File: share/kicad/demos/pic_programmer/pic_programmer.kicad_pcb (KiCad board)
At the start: 2 copper layers, 160 x 99.1 mm, 63 parts, among them J1 DB9-FEMAL, P1 CONN_2, P101 CONN_1, P102 CONN_1, P103 CONN_1, P104 CONN_1, P105 CONN_1, P106 CONN_1, P2 SUPP28, P3 SUPP40, Q1 BC237, Q2 BC307, Q3 BC307, U1 24Cxx, U2 74HC125, U3 7805, U4 LT1373, U5 PIC_18_PINS, U6 PIC_8_PINS

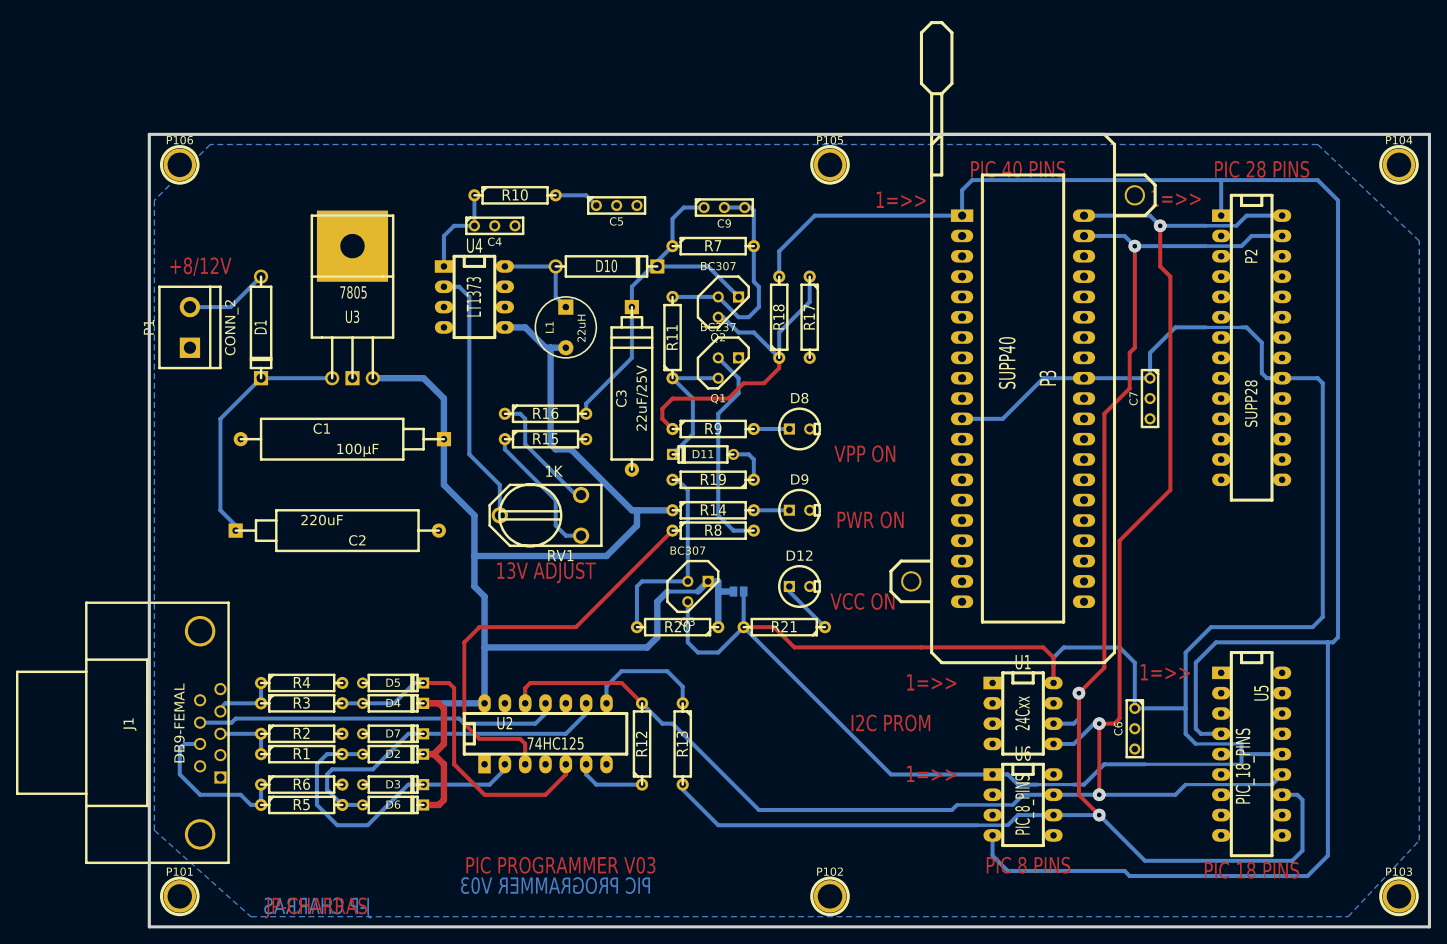
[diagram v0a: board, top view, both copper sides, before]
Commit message: Remove KiCad V4.0.7
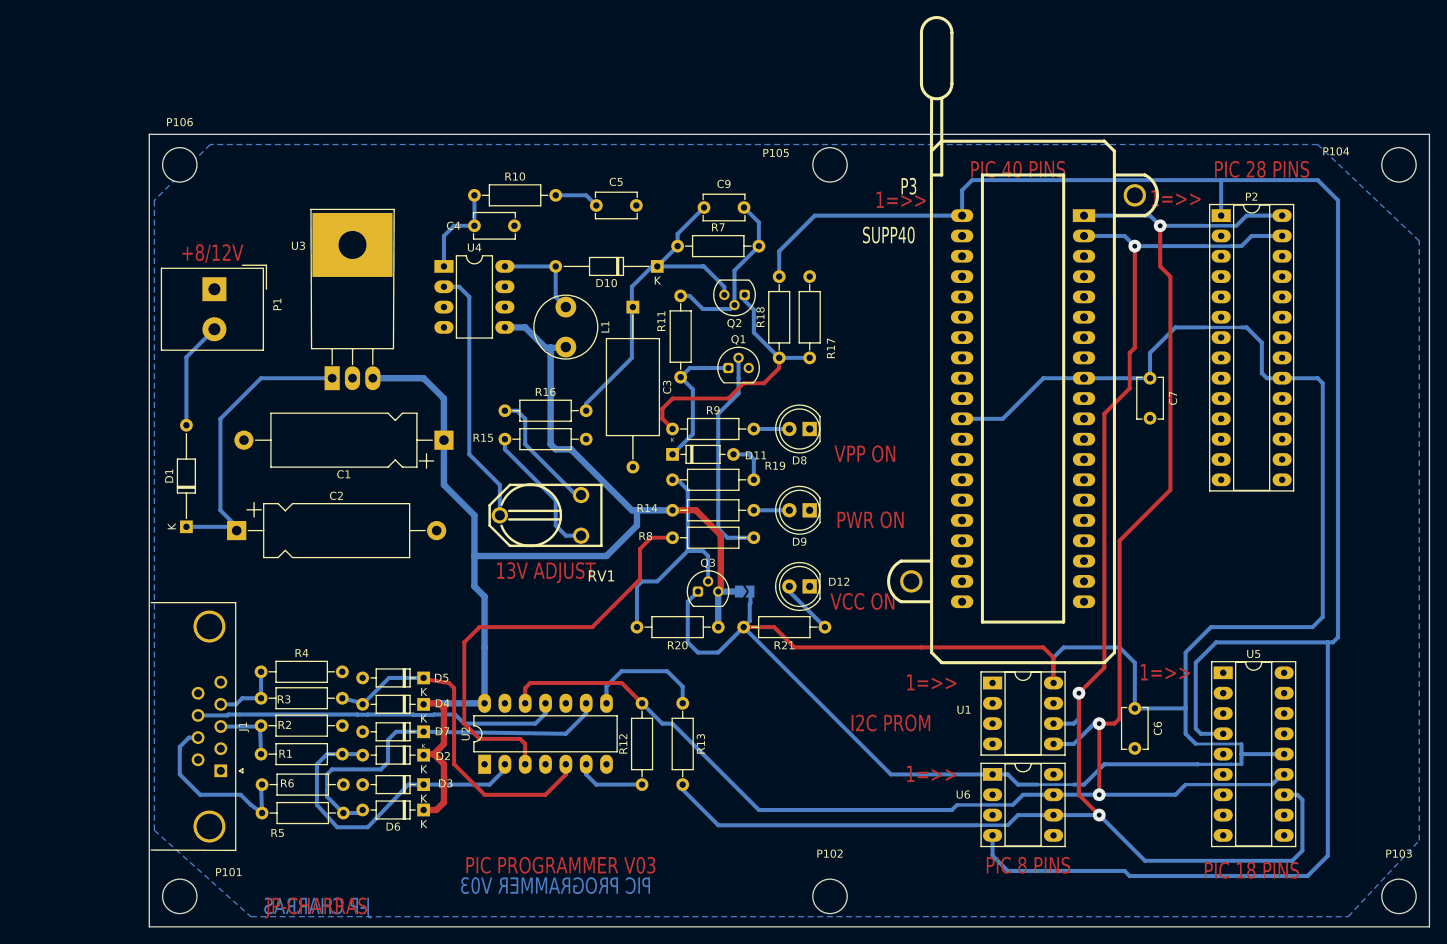
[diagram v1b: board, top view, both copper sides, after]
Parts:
- C1, C2: footprint discret:CP10 -> Capacitor_THT:CP_Axial_L18.0mm_D6.5mm_P25.00mm_Horizontal
- C3: footprint discret:CP8 -> Capacitors_THT:C_Axial_L12.0mm_D6.5mm_P20.00mm_Horizontal
- C4, C5, C6, C7: footprint discret:C1-1 -> Capacitor_THT:C_Disc_D5.1mm_W3.2mm_P5.00mm
- C9: value 22OnF -> 220nF; footprint discret:C1-1 -> Capacitor_THT:C_Disc_D5.1mm_W3.2mm_P5.00mm
- D1, D10: footprint discret:D5 -> Diode_THT:D_DO-35_SOD27_P12.70mm_Horizontal
- D11, D2, D3, D4, D5, D6, D7: footprint discret:D3 -> Diode_THT:D_DO-35_SOD27_P7.62mm_Horizontal
- D12, D8, D9: footprint discret:LEDV -> LED_THT:LED_D5.0mm
- J1: footprint connect:DB9FC -> Connector_Dsub:DSUB-9_Female_Horizontal_P2.77x2.84mm_EdgePinOffset7.70mm_Housed_MountingHolesOffset9.12mm
- JP1: footprint connect:GS2 -> Jumper:SolderJumper-2_P1.3mm_Open_TrianglePad1.0x1.5mm
- L1: footprint inductors:INDUCTOR_V -> Inductor_THT:L_Radial_D7.8mm_P5.00mm_Fastron_07HCP
- P1: footprint connect:bornier2 -> TerminalBlock_Altech:Altech_AK300_1x02_P5.00mm_45-Degree
- P101, P102, P103, P104, P105, P106: footprint footprints:1pin-4 -> MountingHole:MountingHole_4.3mm_M4
- P2: footprint dip_sockets:DIP-28__300_ELL -> Package_DIP:DIP-28_W7.62mm_Socket_LongPads
- P3: footprint sockets:40tex-Ell600 -> footprints:40tex-Ell600
- Q1, Q2, Q3: footprint discret:TO92 -> Package_TO_SOT_THT:TO-92
- R1, R10, R11, R12, R13, R14, R15, R16, R17, R18, R19, R2, R20, R21, R3, R4, R5, R6, R7, R8, R9: footprint discret:R4 -> Resistor_THT:R_Axial_DIN0207_L6.3mm_D2.5mm_P10.16mm_Horizontal
- RV1: footprint discret:RV2X4 -> footprints:RV2X4
- U1, U6: footprint dip_sockets:DIP-8__300_ELL -> Package_DIP:DIP-8_W7.62mm_Socket_LongPads
- U2: footprint dip_sockets:DIP-14__300_ELL -> Package_DIP:DIP-14_W7.62mm_LongPads
- U3: footprint discret:LM78XX -> Package_TO_SOT_THT:TO-220-3_Horizontal_TabDown
- U4: footprint dip_sockets:DIP-8__300_ELL -> Package_DIP:DIP-8_W7.62mm_LongPads
- U5: footprint dip_sockets:DIP-18__300_ELL -> Package_DIP:DIP-18_W7.62mm_Socket_LongPads
- moved D1 26.6 mm to (78.3, 89.7), turned to 90 degrees
- moved P3 25.3 mm to (175.3, 50.8), turned to 0 degrees
- moved P2 16.9 mm to (207.6, 50.8), turned to 0 degrees
- moved C1 12.7 mm to (110.5, 78.9)
- moved C2 12.6 mm to (84.6, 90.2)
- moved U5 10.8 mm to (207.9, 108.0), turned to 0 degrees
- moved C3 10.2 mm to (134.1, 62.2)
- moved U2 8.52 mm to (115.6, 119.4), turned to 90 degrees
- moved D10 6.35 mm to (137.2, 57.1), turned to 180 degrees
- moved RV1 5.68 mm to (127.6, 90.8)
- moved P1 5.67 mm to (81.8, 60.0), turned to -90 degrees
- moved U1 5.39 mm to (179.1, 109.2), turned to 0 degrees
- moved U4 5.39 mm to (110.5, 57.1), turned to 0 degrees
- moved U6 5.39 mm to (179.1, 120.7), turned to 0 degrees
- moved R4 5.27 mm to (87.6, 107.8)
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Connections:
- net /CTS renamed /PC-DATA-IN
- net /DTR renamed /PC-DATA-OUT
- net /TXD renamed /VPP_ON
- net /pic_sockets/CLOCK-RB6 renamed /CLOCK-RB6
- net /pic_sockets/DATA-RB7 renamed /DATA-RB7
- net /pic_sockets/VPP-MCLR renamed /VPP/MCLR
- D1 pad 1: Net-(D1-Pad1) -> Net-(C2-Pad1)
- D1 pad 2: Net-(C2-Pad1) -> Net-(D1-Pad2)
- D10 pad 1: Net-(D10-Pad1) -> VPP
- D10 pad 2: VPP -> Net-(D10-Pad2)
- D12 pad 1: Net-(D12-Pad1) -> GND
- D12 pad 2: GND -> Net-(D12-Pad2)
- D2 pad 1: Net-(D2-Pad1) -> VCC
- D2 pad 2: VCC -> Net-(D2-Pad2)
- D3 pad 1: GND -> Net-(D2-Pad2)
- D3 pad 2: Net-(D2-Pad1) -> GND
- D4 pad 1: Net-(D4-Pad1) -> VCC
- D4 pad 2: VCC -> Net-(D4-Pad2)
- D5 pad 1: GND -> Net-(D4-Pad2)
- D5 pad 2: Net-(D4-Pad1) -> GND
- D6 pad 1: Net-(D6-Pad1) -> VCC
- D6 pad 2: VCC -> Net-(D6-Pad2)
- D7 pad 1: GND -> Net-(D6-Pad2)
- D7 pad 2: Net-(D6-Pad1) -> GND
- D8 pad 1: Net-(D8-Pad1) -> GND
- D8 pad 2: GND -> Net-(D8-Pad2)
- D9 pad 1: Net-(D9-Pad1) -> GND
- D9 pad 2: GND -> Net-(D9-Pad2)
- J1 pad 1: (no net) -> unconnected-(J1-Pad1)
- J1 pad 2: (no net) -> unconnected-(J1-Pad2)
- J1 pad 6: (no net) -> unconnected-(J1-Pad6)
- J1 pad 9: (no net) -> unconnected-(J1-Pad9)
- L1 pad 1: Net-(D10-Pad1) -> Net-(D10-Pad2)
- P1 pad 2: Net-(D1-Pad1) -> Net-(D1-Pad2)
- P2 pad 10: (no net) -> unconnected-(P2-Pad10)
- P2 pad 11: (no net) -> unconnected-(P2-Pad11)
- P2 pad 12: (no net) -> unconnected-(P2-Pad12)
- P2 pad 13: (no net) -> unconnected-(P2-Pad13)
- P2 pad 14: (no net) -> unconnected-(P2-Pad14)
- P2 pad 15: (no net) -> unconnected-(P2-Pad15)
- P2 pad 16: (no net) -> unconnected-(P2-Pad16)
- P2 pad 17: (no net) -> unconnected-(P2-Pad17)
- P2 pad 18: (no net) -> unconnected-(P2-Pad18)
- P2 pad 2: (no net) -> unconnected-(P2-Pad2)
- P2 pad 21: (no net) -> unconnected-(P2-Pad21)
- P2 pad 22: (no net) -> unconnected-(P2-Pad22)
- P2 pad 23: (no net) -> unconnected-(P2-Pad23)
- P2 pad 24: (no net) -> unconnected-(P2-Pad24)
- P2 pad 25: (no net) -> unconnected-(P2-Pad25)
- P2 pad 26: (no net) -> unconnected-(P2-Pad26)
- P2 pad 3: (no net) -> unconnected-(P2-Pad3)
- P2 pad 4: (no net) -> unconnected-(P2-Pad4)
- P2 pad 5: (no net) -> unconnected-(P2-Pad5)
- P2 pad 6: (no net) -> unconnected-(P2-Pad6)
- P2 pad 7: (no net) -> unconnected-(P2-Pad7)
- P2 pad 9: (no net) -> unconnected-(P2-Pad9)
- P3 pad 10: (no net) -> unconnected-(P3-Pad10)
- P3 pad 13: (no net) -> unconnected-(P3-Pad13)
- P3 pad 14: (no net) -> unconnected-(P3-Pad14)
- P3 pad 15: (no net) -> unconnected-(P3-Pad15)
- P3 pad 16: (no net) -> unconnected-(P3-Pad16)
- P3 pad 17: (no net) -> unconnected-(P3-Pad17)
- P3 pad 18: (no net) -> unconnected-(P3-Pad18)
- P3 pad 19: (no net) -> unconnected-(P3-Pad19)
- P3 pad 2: (no net) -> unconnected-(P3-Pad2)
- P3 pad 20: (no net) -> unconnected-(P3-Pad20)
- P3 pad 21: (no net) -> unconnected-(P3-Pad21)
- P3 pad 22: (no net) -> unconnected-(P3-Pad22)
- P3 pad 23: (no net) -> unconnected-(P3-Pad23)
- P3 pad 24: (no net) -> unconnected-(P3-Pad24)
- P3 pad 25: (no net) -> unconnected-(P3-Pad25)
- P3 pad 26: (no net) -> unconnected-(P3-Pad26)
- P3 pad 27: (no net) -> unconnected-(P3-Pad27)
- P3 pad 28: (no net) -> unconnected-(P3-Pad28)
- P3 pad 29: (no net) -> unconnected-(P3-Pad29)
- P3 pad 3: (no net) -> unconnected-(P3-Pad3)
- P3 pad 30: (no net) -> unconnected-(P3-Pad30)
- P3 pad 33: (no net) -> unconnected-(P3-Pad33)
- P3 pad 34: (no net) -> unconnected-(P3-Pad34)
- P3 pad 35: (no net) -> unconnected-(P3-Pad35)
- P3 pad 36: (no net) -> unconnected-(P3-Pad36)
- P3 pad 37: (no net) -> unconnected-(P3-Pad37)
- P3 pad 38: (no net) -> unconnected-(P3-Pad38)
- P3 pad 4: (no net) -> unconnected-(P3-Pad4)
- P3 pad 5: (no net) -> unconnected-(P3-Pad5)
- P3 pad 6: (no net) -> unconnected-(P3-Pad6)
- P3 pad 7: (no net) -> unconnected-(P3-Pad7)
- P3 pad 9: (no net) -> unconnected-(P3-Pad9)
- Q1 pad 1: GND -> Net-(D11-Pad1)
- Q1 pad 3: Net-(D11-Pad2) -> GND
- Q2 pad 1: VPP -> Net-(Q2-Pad1)
- Q2 pad 3: Net-(Q2-Pad3) -> VPP
- Q3 pad 1: VCC -> /pic_sockets/VCC_PIC
- Q3 pad 3: /pic_sockets/VCC_PIC -> VCC
- R1 pad 2: Net-(D2-Pad1) -> Net-(D2-Pad2)
- R11 pad 1: Net-(D11-Pad2) -> Net-(D11-Pad1)
- R14 pad 2: Net-(D9-Pad1) -> Net-(D9-Pad2)
- R17 pad 1: Net-(Q2-Pad3) -> Net-(Q2-Pad1)
- R18 pad 1: Net-(Q2-Pad3) -> Net-(Q2-Pad1)
- R19 pad 1: Net-(D11-Pad1) -> Net-(D11-Pad2)
- R21 pad 1: Net-(D12-Pad1) -> Net-(D12-Pad2)
- R3 pad 2: Net-(D4-Pad1) -> Net-(D4-Pad2)
- R5 pad 2: Net-(D6-Pad1) -> Net-(D6-Pad2)
- R9 pad 1: Net-(Q2-Pad3) -> Net-(Q2-Pad1)
- R9 pad 2: Net-(D8-Pad1) -> Net-(D8-Pad2)
- U1 pad 7: (no net) -> unconnected-(U1-Pad7)
- U2 pad 2: Net-(D2-Pad1) -> Net-(D2-Pad2)
- U2 pad 5: Net-(D4-Pad1) -> Net-(D4-Pad2)
- U2 pad 9: Net-(D6-Pad1) -> Net-(D6-Pad2)
- U4 pad 3: (no net) -> unconnected-(U4-Pad3)
- U4 pad 4: (no net) -> unconnected-(U4-Pad4)
- U4 pad 8: Net-(D10-Pad1) -> Net-(D10-Pad2)
- U5 pad 1: (no net) -> unconnected-(U5-Pad1)
- U5 pad 10: (no net) -> unconnected-(U5-Pad10)
- U5 pad 11: (no net) -> unconnected-(U5-Pad11)
- U5 pad 15: (no net) -> unconnected-(U5-Pad15)
- U5 pad 16: (no net) -> unconnected-(U5-Pad16)
- U5 pad 17: (no net) -> unconnected-(U5-Pad17)
- U5 pad 18: (no net) -> unconnected-(U5-Pad18)
- U5 pad 2: (no net) -> unconnected-(U5-Pad2)
- U5 pad 3: (no net) -> unconnected-(U5-Pad3)
- U5 pad 6: (no net) -> unconnected-(U5-Pad6)
- U5 pad 7: (no net) -> unconnected-(U5-Pad7)
- U5 pad 8: (no net) -> unconnected-(U5-Pad8)
- U5 pad 9: (no net) -> unconnected-(U5-Pad9)
- U6 pad 2: (no net) -> unconnected-(U6-Pad2)
- U6 pad 3: (no net) -> unconnected-(U6-Pad3)
- U6 pad 5: (no net) -> unconnected-(U6-Pad5)
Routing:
- net Net-(D6-Pad2): track 0.00 -> 46.8 mm
- net Net-(D6-Pad1): track 44.0 -> 0.00 mm
- net Net-(D4-Pad2): track 0.00 -> 43.1 mm
- net Net-(D4-Pad1): track 42.7 -> 0.00 mm
- net Net-(Q2-Pad3): track 42.5 -> 0.00 mm
- net Net-(D2-Pad2): track 0.00 -> 39.8 mm
- net Net-(D2-Pad1): track 39.4 -> 0.00 mm
- net Net-(Q2-Pad1): track 0.00 -> 34.5 mm
- net VCC: track 183.3 -> 162.4 mm
- net Net-(D1-Pad2): track 0.00 -> 13.4 mm
- net Net-(D11-Pad1): track 5.34 -> 17.8 mm
- net Net-(D11-Pad2): track 17.3 -> 5.34 mm
- net Net-(D10-Pad2): track 0.00 -> 12.0 mm
- net Net-(D10-Pad1): track 12.0 -> 0.00 mm
- net Net-(D1-Pad1): track 10.5 -> 0.00 mm
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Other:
- net class Default removed
- net class POWER removed
- rule pad_to_mask_clearance: 0.1 -> 0
